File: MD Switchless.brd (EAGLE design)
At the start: 20 x 14.6 mm, 13 parts, among them U1 ATTINY85-20S

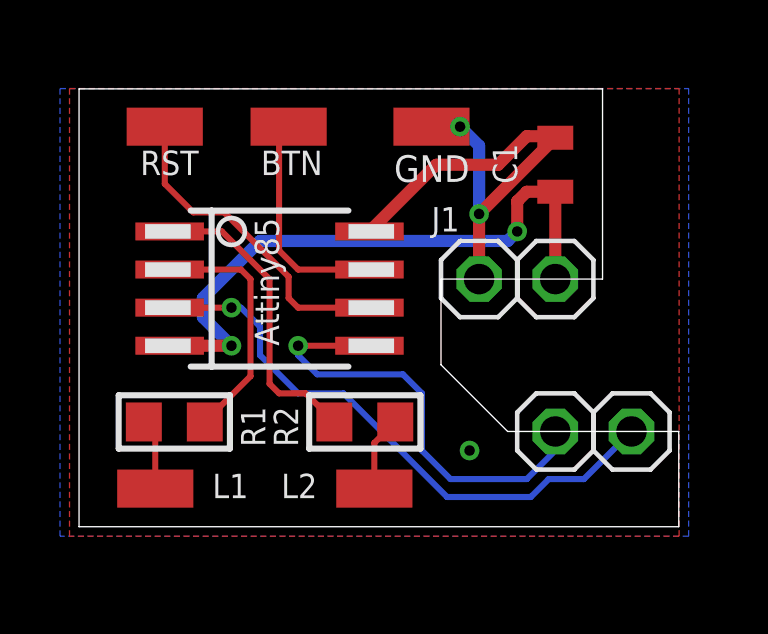
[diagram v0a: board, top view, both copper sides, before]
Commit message: Add files via upload
Minor changes, R1-3 now are 220ohm
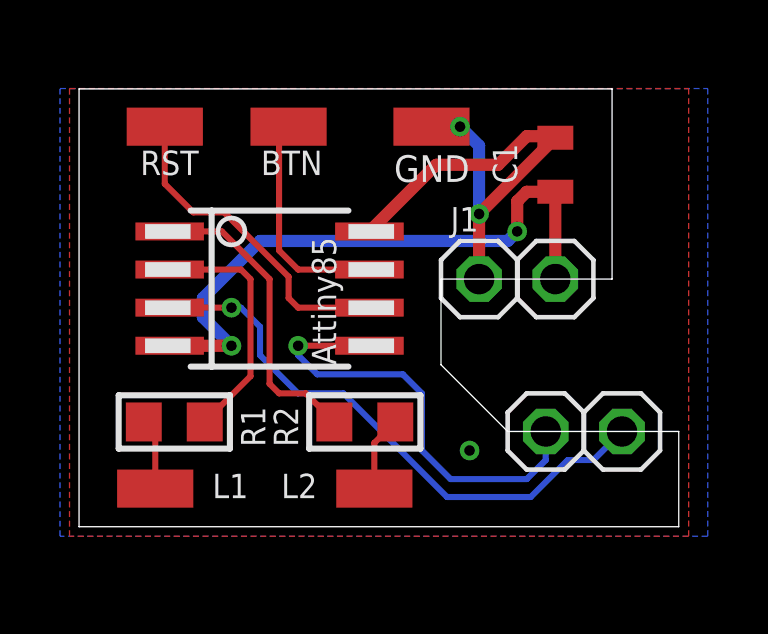
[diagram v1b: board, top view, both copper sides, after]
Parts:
- moved JP5 0.32 mm to (15.6, 3.17)
- moved JP3 0.32 mm to (18.1, 3.17)
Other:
- outline, holes or cut-outs redrawn
- board text added: "C1 100nF R1 220ohm R2 220ohm"
- board text removed: "C1 100nF R1 215ohm R2 215ohm"
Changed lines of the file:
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@@
 <wire x1="0" y1="0" x2="19.99" y2="0" width="0" layer="20"/>
 <wire x1="19.99" y1="0" x2="19.99" y2="3.175" width="0" layer="20"/>
-<wire x1="17.45" y1="8.255" x2="17.45" y2="14.595" width="0" layer="20"/>
-<wire x1="17.45" y1="14.595" x2="0" y2="14.595" width="0" layer="20"/>
+<wire x1="17.7675" y1="8.255" x2="17.7675" y2="14.595" width="0" layer="20"/>
+<wire x1="17.7675" y1="14.595" x2="0" y2="14.595" width="0" layer="20"/>
 <wire x1="0" y1="14.595" x2="0" y2="0" width="0" layer="20"/>
-<wire x1="12.065" y1="8.255" x2="17.45" y2="8.255" width="0" layer="20"/>
+<wire x1="12.065" y1="8.255" x2="17.7675" y2="8.255" width="0" layer="20"/>
 <wire x1="19.99" y1="3.175" x2="14.2875" y2="3.175" width="0" layer="20"/>
 <wire x1="14.2875" y1="3.175" x2="12.065" y2="5.3975" width="0" layer="20"/>
@@
 <text x="4.445" y="0.9525" size="0.8128" layer="25">L1</text>
 <text x="7.9375" y="0.9525" size="0.8128" layer="25" rot="R180" align="top-left">L2</text>
-<text x="11.7475" y="9.8425" size="0.8128" layer="21">J1</text>
+<text x="12.3825" y="9.8425" size="0.8128" layer="21">J1</text>
 <text x="19.05" y="0.635" size="1.016" layer="22" rot="MR0">designed by @kamencesc</text>
 <text x="0.635" y="0.635" size="1.016" layer="22" rot="MR90">MD Switchless MOD</text>
-<text x="6.6675" y="6.0325" size="0.8128" layer="21" rot="R90">Attiny85</text>
+<text x="8.5725" y="5.3975" size="0.8128" layer="21" rot="R90">Attiny85</text>
 <circle x="5.08" y="9.8425" radius="0.4490125" width="0.1524" layer="21"/>
 <rectangle x1="6.1595" y1="4.5085" x2="7.4295" y2="4.7625" layer="22"/>
@@
 <rectangle x1="6.1595" y1="12.3825" x2="6.4135" y2="12.6365" layer="22"/>
 <text x="17.145" y="10.4775" size="0.8128" layer="22" rot="MR0">C1 100nF
-R1 215ohm
-R2 215ohm</text>
+R1 220ohm
+R2 220ohm</text>
 </plain>
 <attributes>
@@
 <attribute name="VALUE" x="14.605" y="5.08" size="1.27" layer="27"/>
 </element>
-<element name="JP3" library="pinhead" library_urn="urn:adsk.eagle:library:325" package="1X01" package3d_urn="urn:adsk.eagle:package:22485/2" value="" x="18.415" y="3.175" smashed="yes">
-<attribute name="VALUE" x="17.145" y="0" size="1.27" layer="27"/>
-</element>
-<element name="JP5" library="pinhead" library_urn="urn:adsk.eagle:library:325" package="1X01" package3d_urn="urn:adsk.eagle:package:22485/2" value="" x="15.875" y="3.175" smashed="yes">
-<attribute name="VALUE" x="14.605" y="0" size="1.27" layer="27"/>
+<element name="JP3" library="pinhead" library_urn="urn:adsk.eagle:library:325" package="1X01" package3d_urn="urn:adsk.eagle:package:22485/2" value="" x="18.0975" y="3.175" smashed="yes">
+<attribute name="VALUE" x="16.8275" y="0" size="1.27" layer="27"/>
+</element>
+<element name="JP5" library="pinhead" library_urn="urn:adsk.eagle:library:325" package="1X01" package3d_urn="urn:adsk.eagle:package:22485/2" value="" x="15.5575" y="3.175" smashed="yes">
+<attribute name="VALUE" x="14.2875" y="0" size="1.27" layer="27"/>
 </element>
 <element name="U1" library="_hhn_attiny25_45_85" package="SOIC8_EIAJ_208MIL" value="ATTINY85-20S" x="6.35" y="7.9375" smashed="yes" rot="R270"/>
@@
 <polygon width="0.2032" layer="1">
 <vertex x="-0.3175" y="14.605"/>
-<vertex x="20.0025" y="14.605"/>
-<vertex x="20.0025" y="-0.3175"/>
+<vertex x="20.32" y="14.605"/>
+<vertex x="20.32" y="-0.3175"/>
 <vertex x="-0.3175" y="-0.3175"/>
 </polygon>
 <polygon width="0.2032" layer="16">
 <vertex x="-0.635" y="14.605"/>
-<vertex x="20.32" y="14.605"/>
-<vertex x="20.32" y="-0.3175"/>
+<vertex x="20.955" y="14.605"/>
+<vertex x="20.955" y="-0.3175"/>
 <vertex x="-0.635" y="-0.3175"/>
 </polygon>
@@
 <wire x1="9.68" y1="6.0325" x2="7.3025" y2="6.0325" width="0.2032" layer="1"/>
 <via x="7.3025" y="6.0325" extent="1-16" drill="0.35"/>
-<wire x1="15.875" y1="3.175" x2="15.875" y2="2.54" width="0.2032" layer="16"/>
-<wire x1="15.875" y1="2.54" x2="14.9225" y2="1.5875" width="0.2032" layer="16"/>
+<wire x1="15.5575" y1="3.175" x2="15.5575" y2="2.2225" width="0.2032" layer="16"/>
+<wire x1="15.5575" y1="2.2225" x2="14.9225" y2="1.5875" width="0.2032" layer="16"/>
 <wire x1="11.43" y1="2.54" x2="11.43" y2="4.445" width="0.2032" layer="16"/>
 <wire x1="11.43" y1="4.445" x2="10.795" y2="5.08" width="0.2032" layer="16"/>
@@
 <wire x1="3.02" y1="7.3025" x2="5.08" y2="7.3025" width="0.2032" layer="1"/>
 <via x="5.08" y="7.3025" extent="1-16" drill="0.35"/>
-<wire x1="18.415" y1="3.175" x2="16.8275" y2="1.5875" width="0.2032" layer="16"/>
-<wire x1="16.8275" y1="1.5875" x2="15.6525" y2="1.5875" width="0.2032" layer="16"/>
-<wire x1="15.6525" y1="1.5875" x2="15.0556" y2="0.9906" width="0.2032" layer="16"/>
+<wire x1="18.0975" y1="3.175" x2="17.145" y2="2.2225" width="0.2032" layer="16"/>
+<wire x1="17.145" y1="2.2225" x2="16.2875" y2="2.2225" width="0.2032" layer="16"/>
+<wire x1="16.2875" y1="2.2225" x2="15.0556" y2="0.9906" width="0.2032" layer="16"/>
 <wire x1="15.0556" y1="0.9906" x2="12.2667625" y2="0.9906" width="0.2032" layer="16"/>
 <wire x1="8.8123625" y1="4.445" x2="7.3025" y2="4.445" width="0.2032" layer="16"/>

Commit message: Add files via upload
traces and pinout changes
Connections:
- net N$5 renamed L1
- net N$6 renamed L2
- removed net N$1: R2.1, U1.1
- removed net N$2: R1.1, U1.2
- new net RL1: R1.1, U1.6
- new net RL2: R2.1, U1.5
- net BTN: now also U1.2; no longer U1.7
- net LENG: now also U1.7; no longer U1.5
- net RST: now also U1.1; no longer U1.6
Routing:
- net N$1: track 10.2 -> 0.00 mm
- net RL1: track 0.00 -> 8.74 mm
- net N$2: track 8.22 -> 0.00 mm
- net RST: track 10.9 -> 3.56 mm
- net RL2: track 0.00 -> 6.38 mm
- net LENG: track 15.0 -> 10.2 mm, vias 1 -> 0
- net GND: track 17.4 -> 15.6 mm, vias 3 -> 2
- net HERZ: track 19.2 -> 20.4 mm
- net 5V: track 20.8 -> 20.0 mm
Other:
- outline, holes or cut-outs redrawn
